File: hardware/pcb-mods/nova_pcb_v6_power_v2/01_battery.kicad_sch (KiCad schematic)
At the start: 4 parts, among them J1 XT60_4S_IN, M1 Voltmeter_DC, Q1 IRLB3034PBF, SW1 Rocker_30A

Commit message: pcb(v6-power-v2): backfill MPN + Manufacturer fields — 100% BOM coverage
All 50 BOM components now carry MPNs from the verified order list:
Yageo RC0603 resistor set (R14 470k = Vishay CRCW0603 DigiKey sub),
Nichicon UPW1E bulk caps, Bourns SRR1260-220M, Infineon IRLB3034PBF,
onsemi BSS138 x3, TI LM393DR, Pololu buck modules (off-board),
GODIY INA226 20A R002 modules with I2C addresses in Manufacturer field,
AMASS XT60H/XT30U, JST B3B-XH-A, Adam Tech BHR-12-VUA, Sullins headers.
ERC: 0 errors (1 expected V7V5_ARM warning). kicad-happy bom_lock: pass.

Co-Authored-By: Claude Fable 5 <noreply@anthropic.com>
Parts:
- J1: MPN (none) -> XT60H-M; Manufacturer (none) -> AMASS
- M1: MPN (none) -> PRPC040SAAN-RC; Manufacturer (none) -> Sullins (snap to 1x02)
- Q1: MPN (none) -> IRLB3034PBF; Manufacturer (none) -> Infineon
- SW1: MPN (none) -> KF301-5.0-2P; Manufacturer (none) -> Generic (Tugermoola kit; SW1 wires to Blue Sea Contura)
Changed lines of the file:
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@@
+			)
+		)
+		(property "Manufacturer" "Sullins (snap to 1x02)" (at 0 0 0)
+			(effects
+				(font
+					(size 1.27 1.27)
+				)
+				(hide yes)
+			)
+		)
+		(property "MPN" "PRPC040SAAN-RC" (at 0 0 0)
+			(effects
+				(font
+					(size 1.27 1.27)
+				)
+				(hide yes)
 			)
 		)
@@
 					(size 1.27 1.27)
 				)
+			)
+		)
+		(property "Manufacturer" "Generic (Tugermoola kit; SW1 wires to Blue Sea Contura)" (at 0 0 0)
+			(effects
+				(font
+					(size 1.27 1.27)
+				)
+				(hide yes)
+			)
+		)
+		(property "MPN" "KF301-5.0-2P" (at 0 0 0)
+			(effects
+				(font
+					(size 1.27 1.27)
+				)
+				(hide yes)
 			)
 		)
@@
 			)
 		)
+		(property "Manufacturer" "AMASS" (at 0 0 0)
+			(effects
+				(font
+					(size 1.27 1.27)
+				)
+				(hide yes)
+			)
+		)
+		(property "MPN" "XT60H-M" (at 0 0 0)
+			(effects
+				(font
+					(size 1.27 1.27)
+				)
+				(hide yes)
+			)
+		)
 		(pin "1"
 		)
@@
 			)
 		)
+		(property "Manufacturer" "Infineon" (at 0 0 0)
+			(effects
+				(font
+					(size 1.27 1.27)
+				)
+				(hide yes)
+			)
+		)
+		(property "MPN" "IRLB3034PBF" (at 0 0 0)
+			(effects
+				(font
+					(size 1.27 1.27)
+				)
+				(hide yes)
+			)
+		)

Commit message: pcb(v6-power-v2): correct C1-C5 to FymuSing (as purchased) + DigiKey PNs from order CSV
Verified against Complete_Digikey_Order_NOVA.csv (16 lines, all match):
R14 470k confirmed Vishay CRCW0603470KFKEA (541-470KHCT-ND).
C1-C5 corrected Nichicon->FymuSing 1000uF/25V (Amazon purchase, 10x17mm).
Remaining 23 parts without DigiKey PN are Amazon/Pololu/AMASS sourced.

Co-Authored-By: Claude Fable 5 <noreply@anthropic.com>
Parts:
- M1: DigiKey (none) -> S1011EC-40-ND
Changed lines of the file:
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@@
+			)
+		)
+		(property "DigiKey" "S1011EC-40-ND" (at 0 0 0)
+			(effects
+				(font
+					(size 1.27 1.27)
+				)
+				(hide yes)
 			)
 		)

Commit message: pcb(v6-power-v2): AssemblyOrder fields + assembly-sequenced iBOM
15-step hand-solder sequence (flat->tall, SMD bottom cluster -> THT top):
0603s -> SOT-23 -> SOIC -> L1 -> INA headers -> headers/JST/IDC ->
screw blocks -> XT30 -> XT60 -> Q1 (Step 10a test first) -> 470uF -> 1000uF.
bom/ibom_assembly.html groups by AssemblyOrder via netlist extra-data.

Co-Authored-By: Claude Fable 5 <noreply@anthropic.com>
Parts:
- J1: AssemblyOrder (none) -> 12 THT XT60 (snap cover off first)
- M1: AssemblyOrder (none) -> 07 THT pin header
- Q1: AssemblyOrder (none) -> 13 THT TO-220 (test per Step 10a FIRST)
- SW1: AssemblyOrder (none) -> 10 THT screw block
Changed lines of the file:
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@@
+			)
+		)
+		(property "AssemblyOrder" "07 THT pin header" (at 0 0 0)
+			(effects
+				(font
+					(size 1.27 1.27)
+				)
+				(hide yes)
 			)
 		)
@@
 		)
 		(property "MPN" "KF301-5.0-2P" (at 0 0 0)
+			(effects
+				(font
+					(size 1.27 1.27)
+				)
+				(hide yes)
+			)
+		)
+		(property "AssemblyOrder" "10 THT screw block" (at 0 0 0)
 			(effects
 				(font
@@
 			)
 		)
+		(property "AssemblyOrder" "12 THT XT60 (snap cover off first)" (at 0 0 0)
+			(effects
+				(font
+					(size 1.27 1.27)
+				)
+				(hide yes)
+			)
+		)
 		(pin "1"
 		)
@@
 			(effects
 				(font
+					(size 1.27 1.27)
+				)
+				(hide yes)
+			)
+		)
+		(property "AssemblyOrder" "13 THT TO-220 (test per Step 10a FIRST)" (at 0 0 0)
+			(effects
+				(font

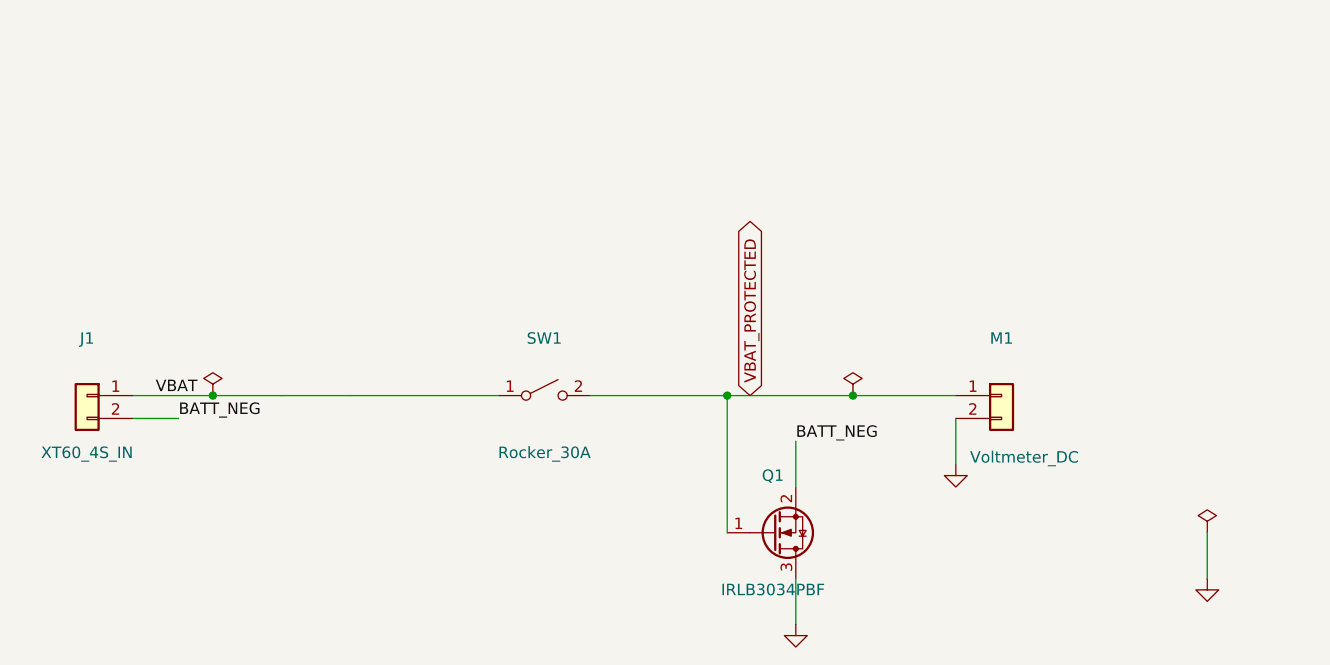
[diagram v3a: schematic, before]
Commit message: Chassis + leg_v6 CAD: no-drill assembly, leg fault audit (LA-1..28 + #47), fastener + gate hardening (#48)
* power board: arm Phase-4 routed + cleaned + fresh gerbers (fab-ready)

Completes the power board (blocker B1):
- U5.EN routed on EN_BUCKS (re-gate now realized on the board).
- V7V5_ARM 3mm, BATT_NEG/VBAT long runs 3mm, 21 high-current pads solid
  zone-connection (current-capacity fixes; TO-220/SW1 escapes left at 1.3mm).
- Removed the duplicate U12 + J14 (F8 UUID-mismatch artifacts) and the full
  orphan dangling-track chain they left behind.
- DRC: 0 hard, 0 unconnected, 0 dangling (10 cosmetic silk/lib only).
- Gerbers regenerated; fab_gate GO on both boards (J20 cross-board match OK).

DNP roster correct (U5 arm buck, U12 arm INA = Phase-4 reserve).

Co-Authored-By: Claude Opus 4.8 <noreply@anthropic.com>

* audit fixes 2026-06-18: NaN guard, pinout/battery/LVC doc sync, STATUS audit block

- main.cpp: NaN guard on commanded position (was UB (uint16_t)NaN -> 0 slam)
- teensy firmware/README.md: pinout table corrected to match main.cpp/PCB v6 (Serial1 0/1, E-stop 5, batt 4, active-LOW OE)
- power-budget.md + BOM.md: battery 4000->6000mAh (real Ovonic packs) + runtime/charge recompute
- BOM.md: bus driver order line -> SN74LVC125A (must be LVC, not 74HC125)
- STATUS.md: cross-domain audit section (open misalignments, weak points, questions)

Co-Authored-By: Claude Opus 4.8 <noreply@anthropic.com>

* docs: add servo-bus half-duplex timing bench checklist (pre-power-on §10)

Co-Authored-By: Claude Opus 4.8 <noreply@anthropic.com>

* docs: battery 4000->6000mAh sweep across secondary docs + STATUS CI-note fix

- 6000mAh 4S Ovonic (real pack) in cad-tooling, notes-qol (SoC math 5400mAh),
  order-list (bag), wiring diagram, README charger note, patterns pocket label
- dimensions.md + patterns.md: physical box/pocket dims flagged RE-MEASURE
  (6000mAh pack is larger; old 4000mAh dims kept as reference, not as truth)
- STATUS.md: corrected CI note (ros-pytest.yml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
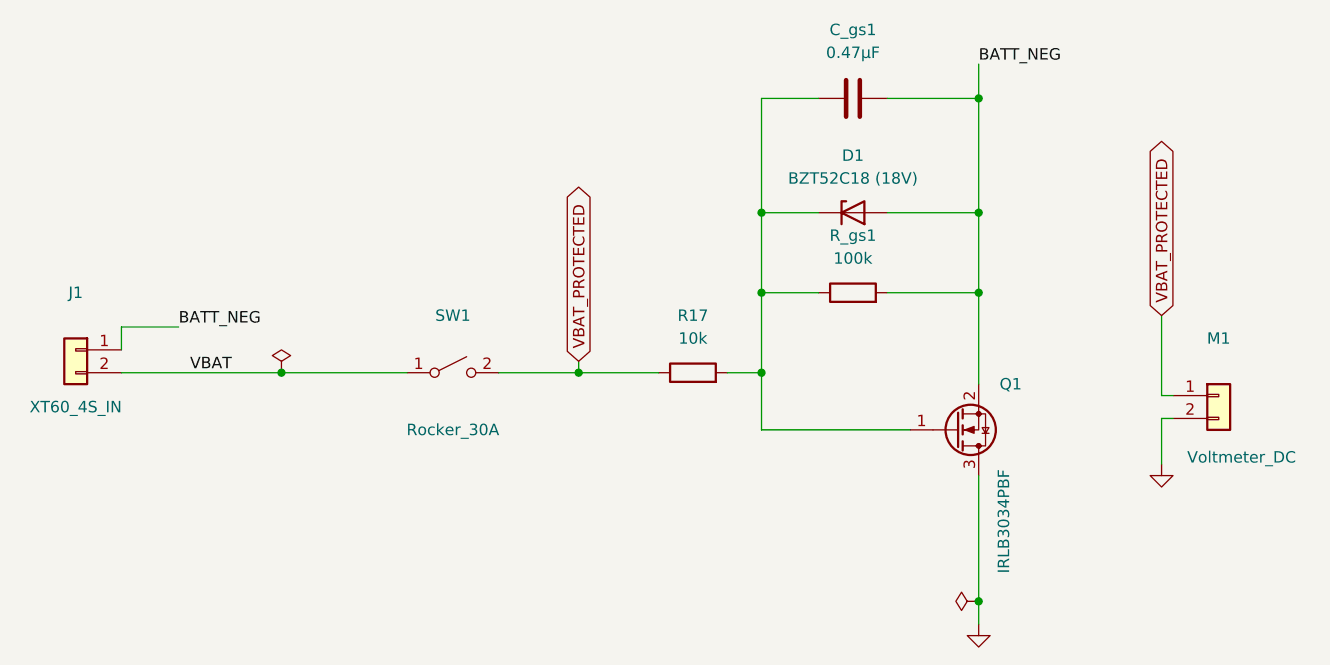
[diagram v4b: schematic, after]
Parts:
- added C_gs1: 0.47μF, Capacitor_SMD:C_0603_1608Metric, symbol Device:C
- added D1: BZT52C18 (18V), Diode_SMD:D_SOD-123F, symbol Device:D_Zener
- added R17: 10k, Resistor_SMD:R_0603_1608Metric, symbol Device:R
- added R_gs1: 100k, Resistor_SMD:R_0603_1608Metric, symbol Device:R
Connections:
- net BATT_NEG: now also J1.1 (Pin_1), C_gs1.2, D1.2 (A), R_gs1.2; no longer J1.2 (Pin_2)
- net VBAT: now also J1.2 (Pin_2); no longer J1.1 (Pin_1)
- net VBAT_PROTECTED: now also R17.1; no longer Q1.1 (G)
- new net: C_gs1.1, D1.1 (K), Q1.1 (G), R17.2, R_gs1.1
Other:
- moved on the sheet: J1, M1, Q1, SW1
